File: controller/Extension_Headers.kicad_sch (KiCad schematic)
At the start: 3 parts

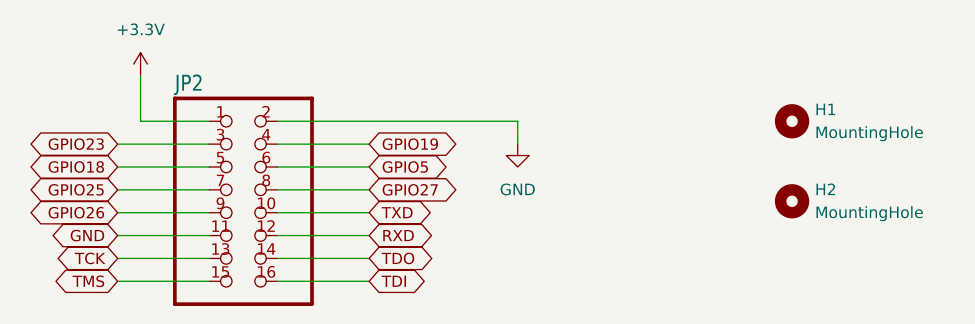
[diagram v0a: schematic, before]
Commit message: Cleaned up controller
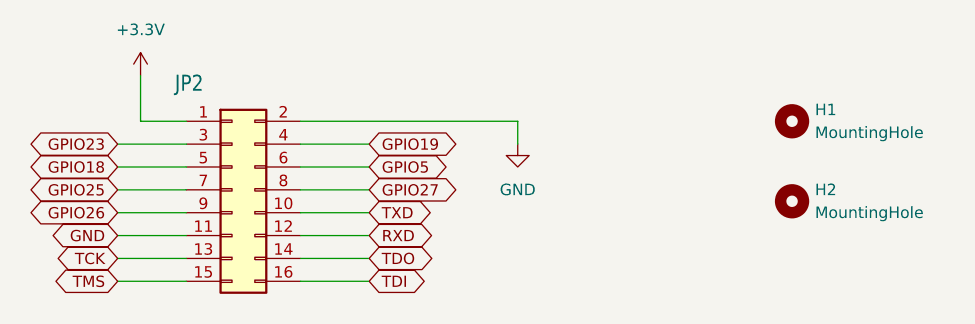
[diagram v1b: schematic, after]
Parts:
- JP2: symbol controller-eagle-import:PINHD-2X8 -> Connector_Generic:Conn_02x08_Odd_Even
